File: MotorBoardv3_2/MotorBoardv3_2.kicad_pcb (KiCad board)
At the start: 2 copper layers, 128.3 x 158.1 mm, 97 parts, among them J1 Bump0, J11 GP2Y0A41SK0F, J12 GP2Y0A41SK0F, J13 GP2Y0A41SK0F, J15 7.2, J16 LP5.0, J17 ELA, J18 ERA, J19 Voltage Display Port, J2 Bump1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

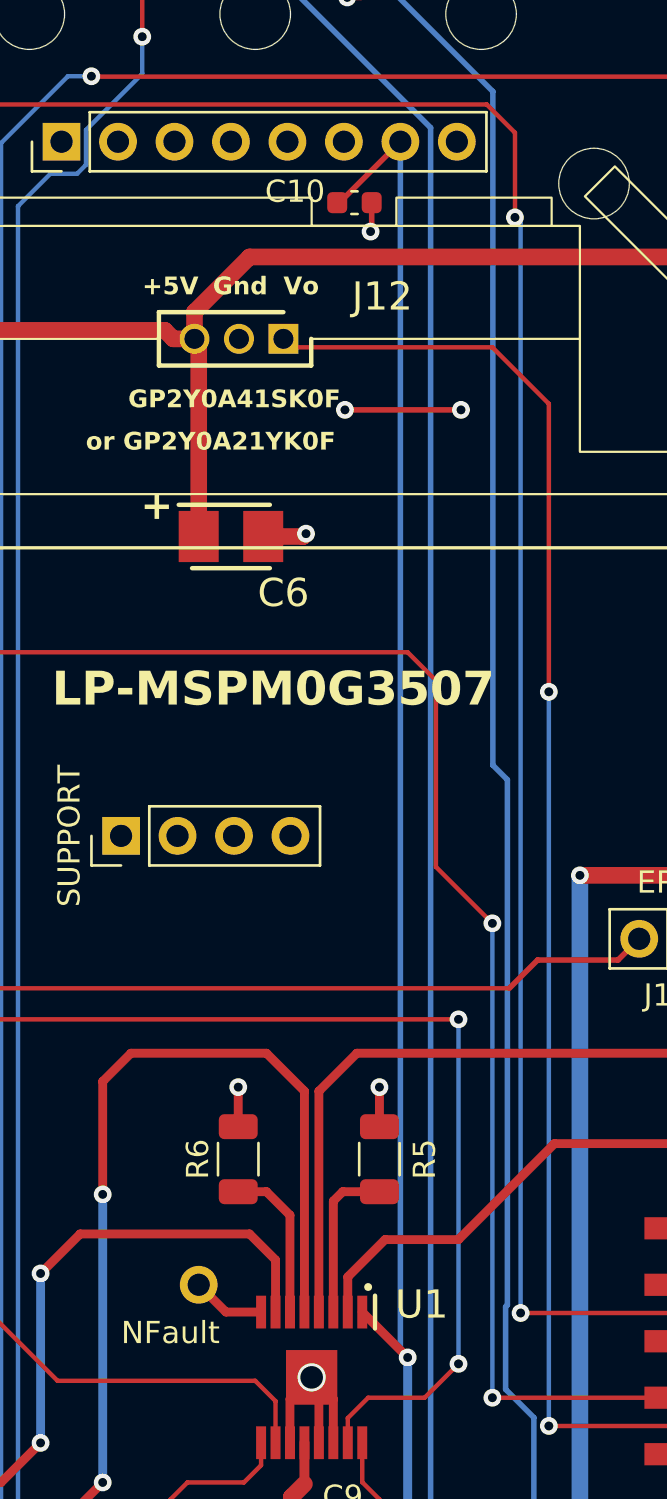
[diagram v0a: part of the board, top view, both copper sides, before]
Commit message: Increased trace widths
Increased trace widths of 3.3V and GND signals going to Bluetooth module
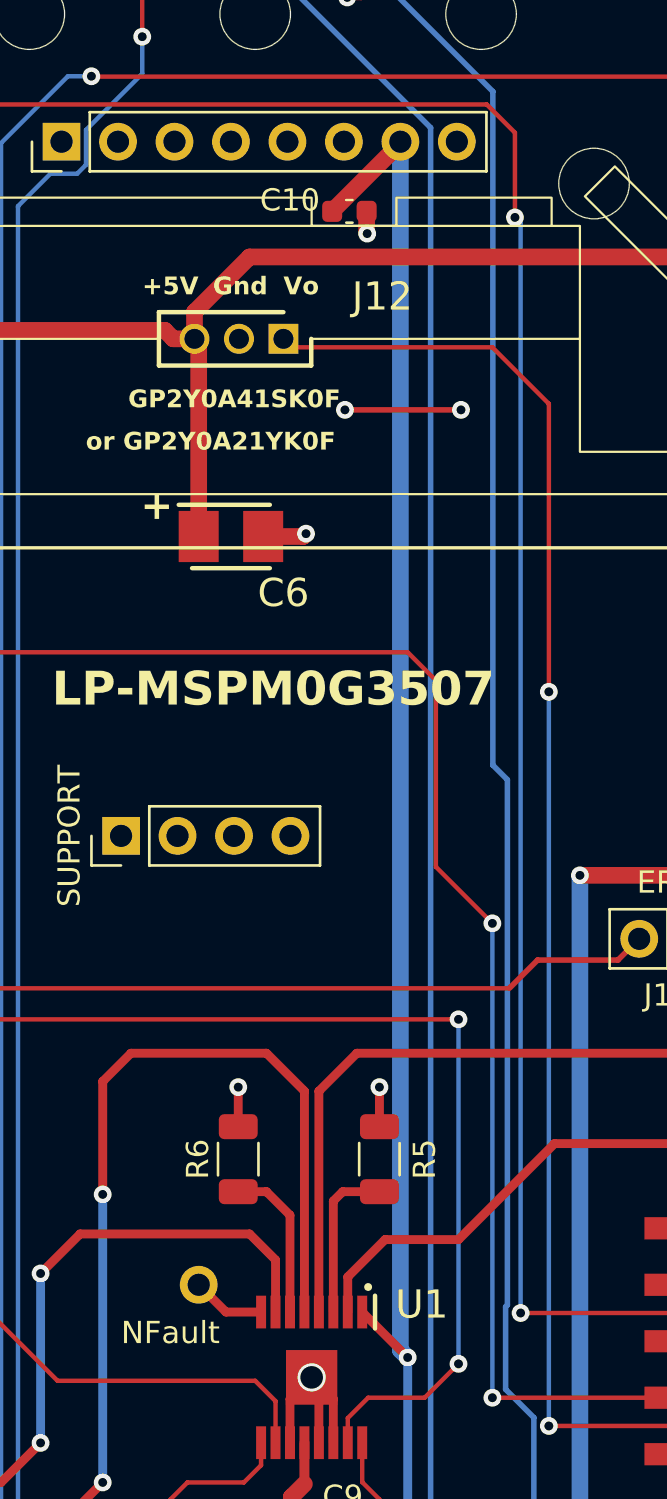
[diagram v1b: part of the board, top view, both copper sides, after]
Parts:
- moved C10 0.45 mm to (113.5, 52.0)
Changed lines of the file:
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@@
 	(footprint "RSLK2:C_0603_1608Metric"
 		(layer "F.Cu")
-		(at 113.685 51.66)
+		(at 113.457 52.05)
 		(descr "Capacitor SMD 0603 (1608 Metric), square (rectangular) end terminal, IPC_7351 nominal, (Body size source: IPC-SM-782 page 76, https://www.pcb-3d.com/wordpress/wp-content/uploads/ipc-sm-782a_amendment_1_and_2.pdf), generated with kicad-footprint-generator")
 		(tags "capacitor")
@@
 	)
 	(segment
-		(start 114.46 52.91)
-		(end 114.46 51.66)
-		(width 0.25)
+		(start 114.232 53.025)
+		(end 114.257 53.05)
+		(width 0.75)
 		(layer "F.Cu")
 		(net 1)
@@
 	)
 	(segment
-		(start 114.41 52.96)
-		(end 114.46 52.91)
-		(width 0.25)
-		(layer "F.Cu")
-		(net 1)
-	)
-	(segment
 		(start 82.804 78.56)
 		(end 78.165 78.56)
@@
 	)
 	(segment
+		(start 114.232 52.05)
+		(end 114.232 53.025)
+		(width 0.75)
+		(layer "F.Cu")
+		(net 1)
+	)
+	(segment
 		(start 81.78 168.87)
 		(end 81.78 168.09)
@@
 	)
 	(via
+		(at 114.257 53.05)
+		(size 0.8)
+		(drill 0.4)
+		(layers "F.Cu" "B.Cu")
+		(net 1)
+	)
+	(via
 		(at 113.792 111.252)
 		(size 0.8)
@@
 	)
 	(via
-		(at 114.41 52.96)
-		(size 0.8)
-		(drill 0.4)
-		(layers "F.Cu" "B.Cu")
-		(net 1)
-	)
-	(via
 		(at 108.458 91.44)
 		(size 0.8)
@@
 	)
 	(segment
+		(start 115.75 48.982)
+		(end 112.682 52.05)
+		(width 0.75)
+		(layer "F.Cu")
+		(net 2)
+	)
+	(segment
 		(start 75.311 122.555)
 		(end 78.486 125.73)
@@
 	)
 	(segment
-		(start 115.75 48.92)
-		(end 113.01 51.66)
-		(width 0.25)
-		(layer "F.Cu")
-		(net 2)
-	)
-	(segment
 		(start 148.463 115.57)
 		(end 149.225 115.57)
@@
 	)
 	(segment
-		(start 113.01 51.66)
-		(end 112.91 51.66)
-		(width 0.25)
+		(start 63.525 127.66)
+		(end 62.865 127)
+		(width 0.2)
 		(layer "F.Cu")
 		(net 2)
 	)
 	(segment
-		(start 63.525 127.66)
-		(end 62.865 127)
-		(width 0.2)
+		(start 115.75 48.92)
+		(end 115.75 48.982)
+		(width 0.75)
 		(layer "F.Cu")
 		(net 2)
@@
 	)
 	(segment
-		(start 115.75 48.92)
-		(end 115.75 103.272)
-		(width 0.25)
-		(layer "B.Cu")
-		(net 2)
-	)
-	(segment
 		(start 71.12 120.65)
 		(end 71.12 122.555)
@@
 		(start 115.75 103.272)
 		(end 116.078 103.6)
-		(width 0.25)
+		(width 0.75)
 		(layer "B.Cu")
 		(net 2)
@@
 		(layer "B.Cu")
 		(net 2)
+	)
+	(segment
+		(start 115.75 48.92)
+		(end 115.75 103.272)
+		(width 0.75)
+		(layer "B.Cu")
+		(net 2)

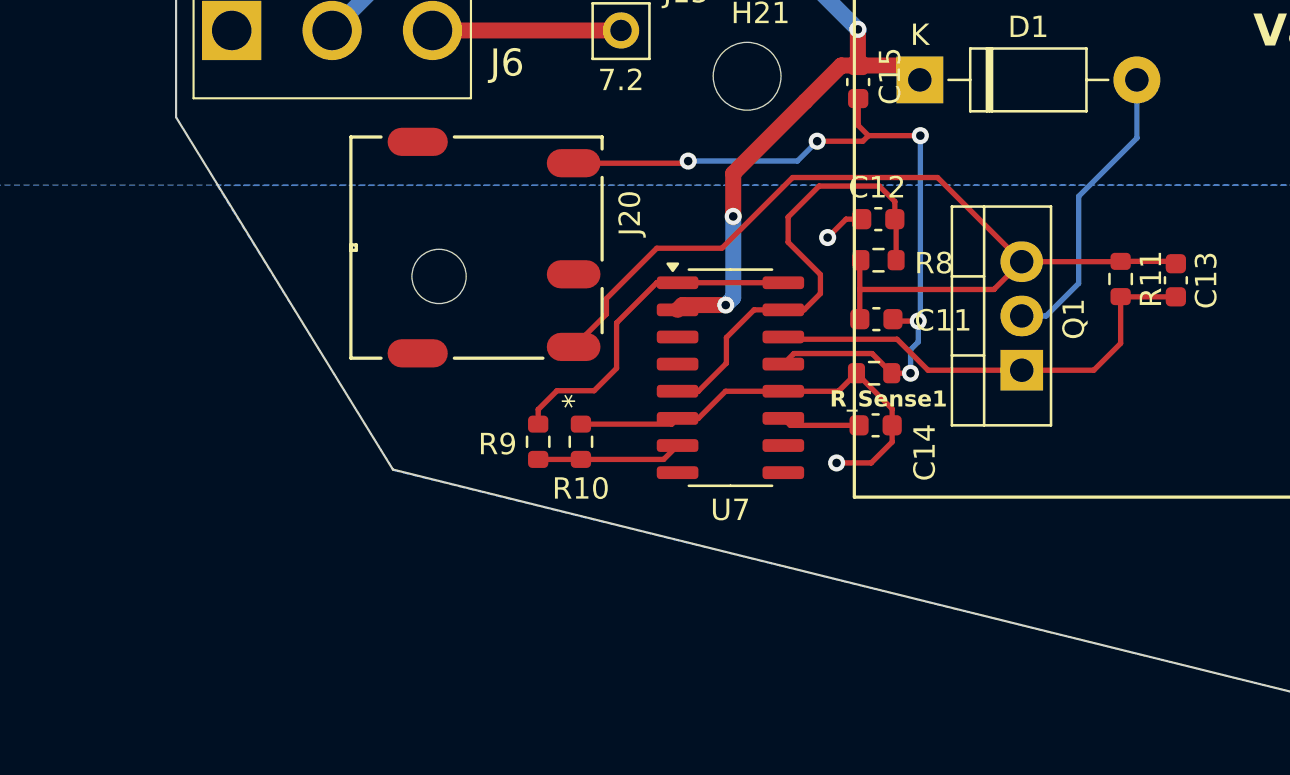
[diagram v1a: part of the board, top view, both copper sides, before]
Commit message: Added test points to Charge Circuit
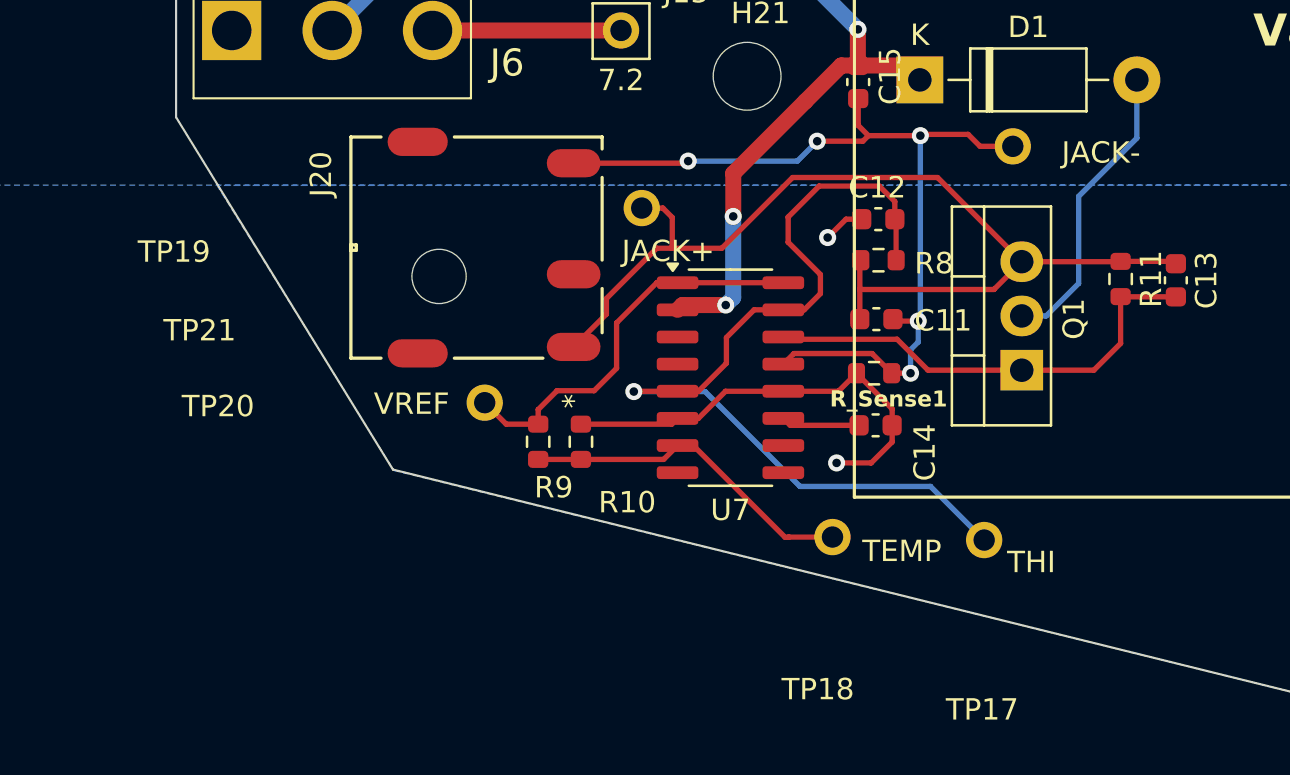
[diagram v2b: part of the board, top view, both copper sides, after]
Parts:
- added TP17: THI, RSLK2:Testpoint_1x1, F.Cu at (86.1, 173.5)
- added TP18: TEMP, RSLK2:Testpoint_1x1, F.Cu at (79.0, 173.3)
- added TP19: JACK+, RSLK2:Testpoint_1x1, F.Cu at (70.1, 157.9)
- added TP20: VREF, RSLK2:Testpoint_1x1, F.Cu at (62.7, 167.0)
- added TP21: JACK-, RSLK2:Testpoint_1x1, F.Cu at (87.4, 155.0)
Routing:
- net /Charge Circuit/V+: track 22.6 -> 44.0 mm, vias 0 -> 1
- net /Charge Circuit/TEMP: track 6.79 -> 16.0 mm
- net Net-(TP21-A): track 37.8 -> 42.4 mm
- net Net-(Q1-E): track 44.5 -> 47.5 mm
- net /Charge Circuit/REF: track 15.9 -> 18.8 mm

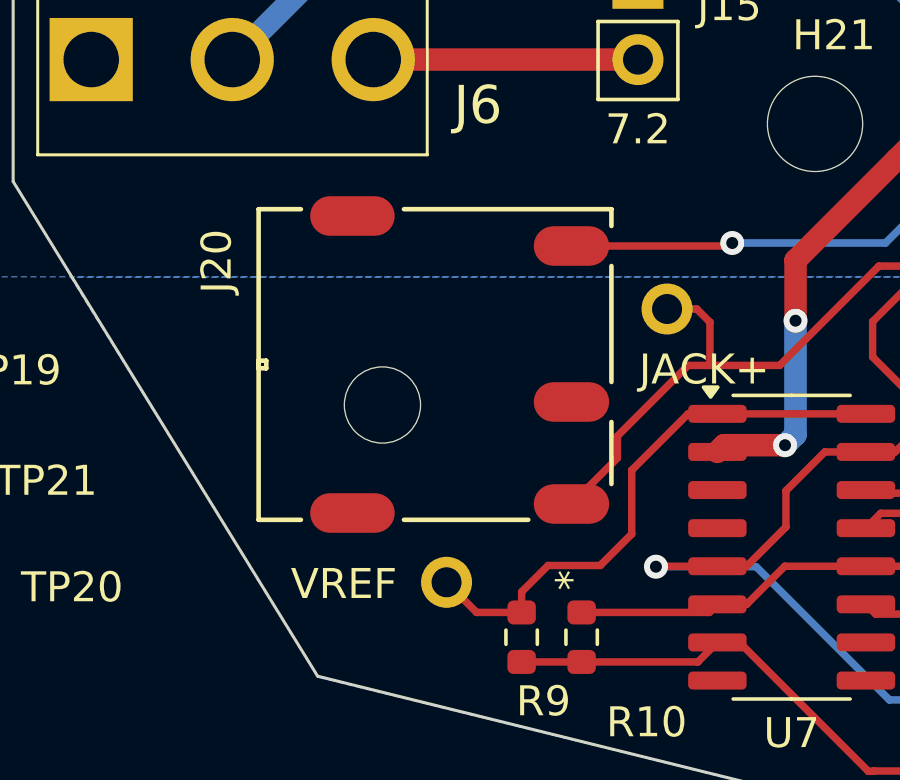
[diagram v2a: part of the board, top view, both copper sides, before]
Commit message: Changed Barrel Jack Footprint to incorporate through-hole connections
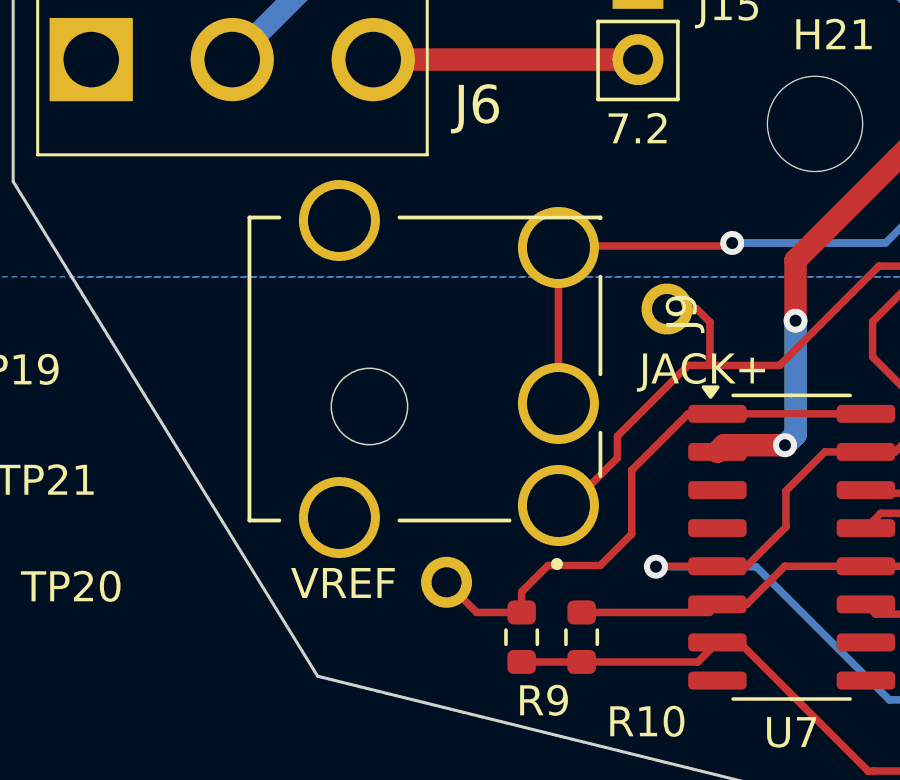
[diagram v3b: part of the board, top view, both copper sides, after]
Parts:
- removed J20: Barrel_Jack, RSLK2:54-00127_TEN
- added J9: 54-00127, RSLK2:TENSILITY_54-00127, F.Cu at (59.1, 159.9)
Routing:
- net Net-(TP21-A): track 42.4 -> 47.6 mm

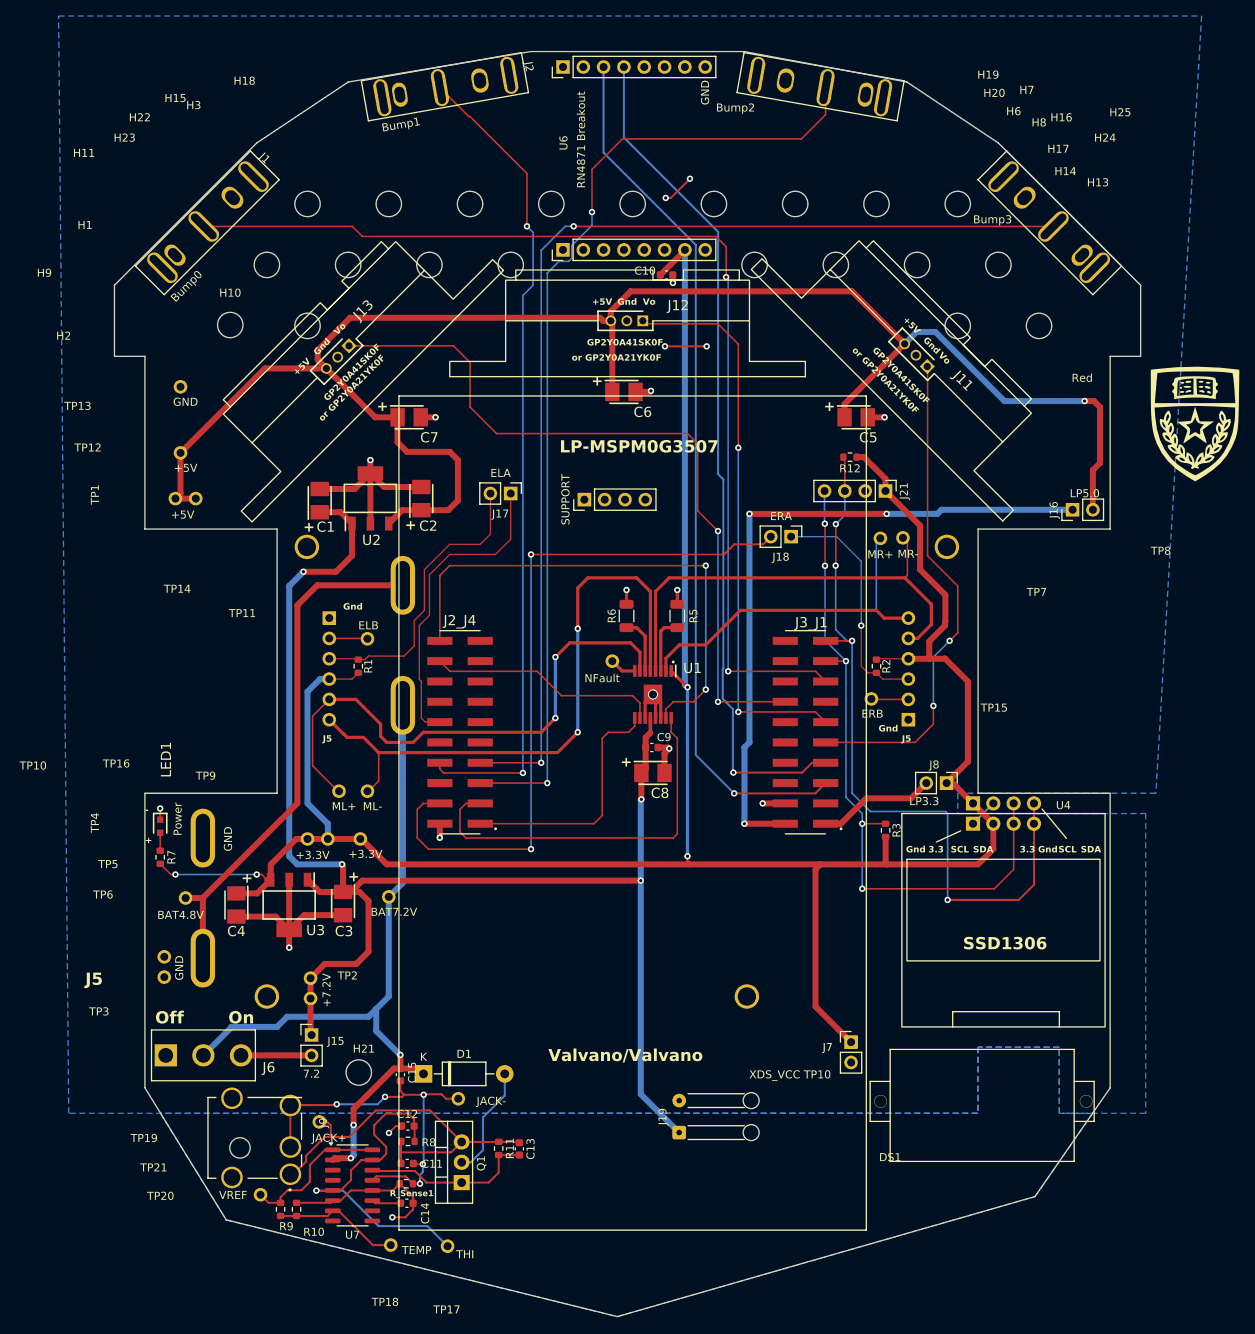
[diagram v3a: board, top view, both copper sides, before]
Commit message: Updated Labeling so Silkscreen is not offboard; Added some necessary changes
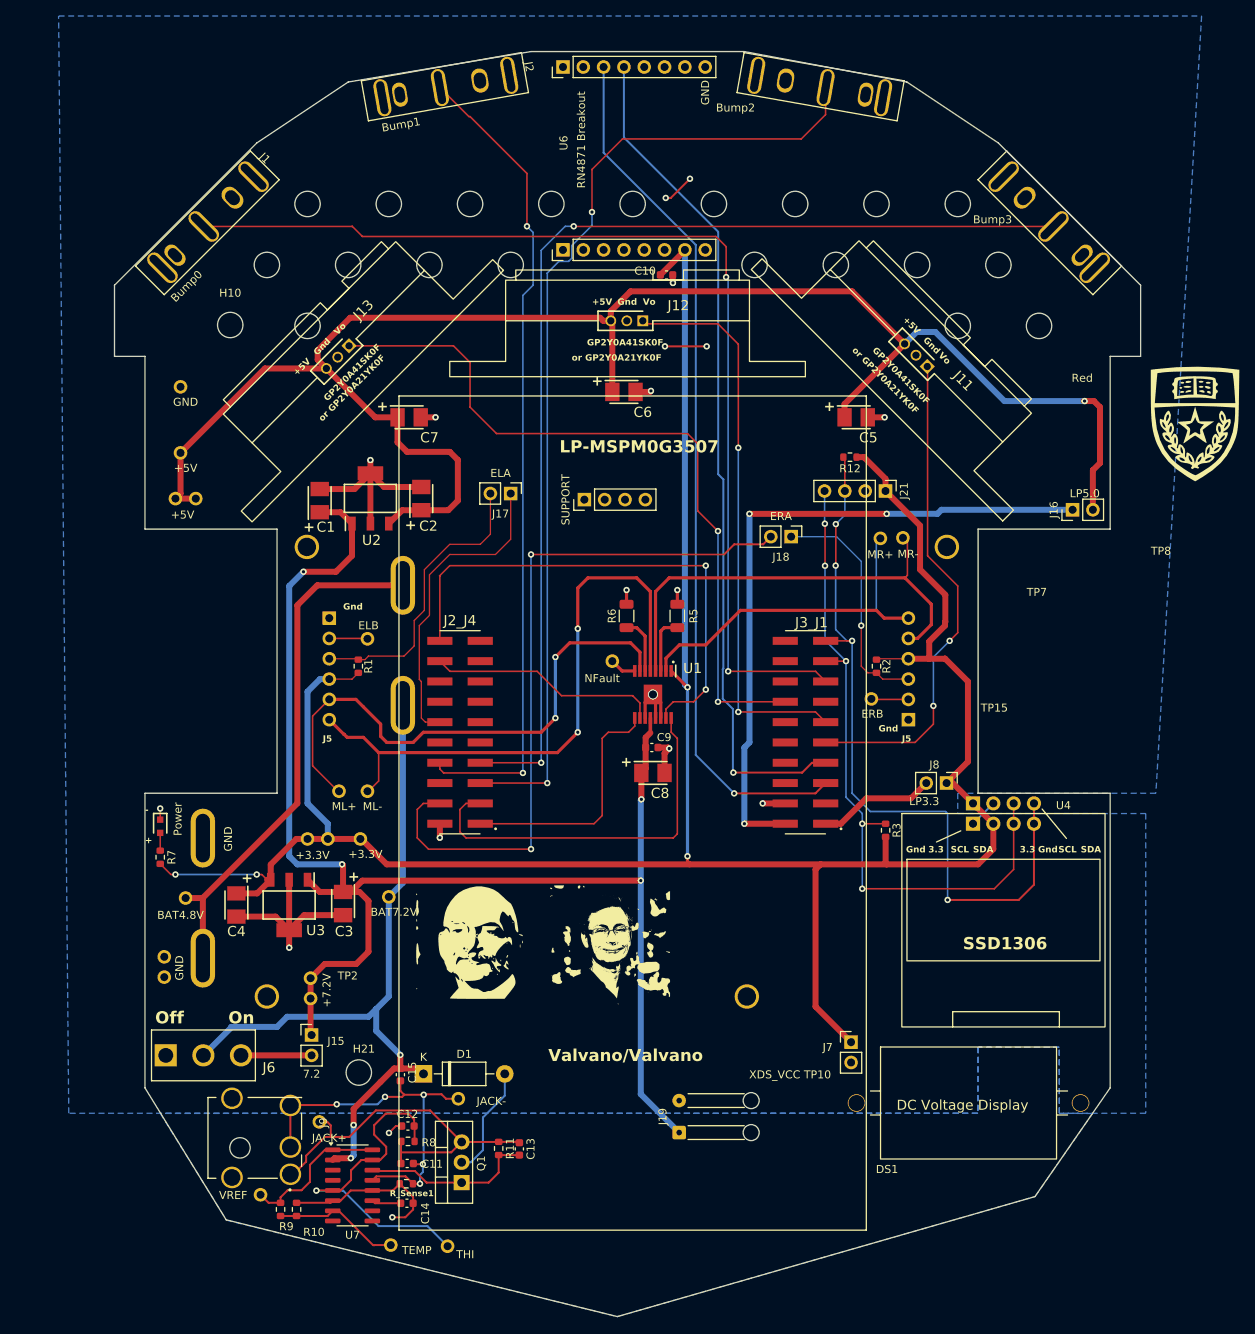
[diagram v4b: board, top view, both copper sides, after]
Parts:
- added G***: LOGO, RSLK2:ToddDelong, F.Cu at (89.7, 135.0)
- added G***: LOGO, RSLK2:AdamBarnes, F.Cu at (106.4, 135.9)
- moved DS1 1.71 mm to (139.7, 163.1)
